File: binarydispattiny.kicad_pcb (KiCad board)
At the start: 2 copper layers, 61.8 x 40.5 mm, 32 parts, among them J1 Conn_01x02_Male, J2 Conn_01x08, J3 AVR-TPI-6, Q1 DMMT5401, U1 4021, U2 ATtiny102-SS, U3 19x12mm 7segment, U4 MAX7219, U5 19x12mm 7segment

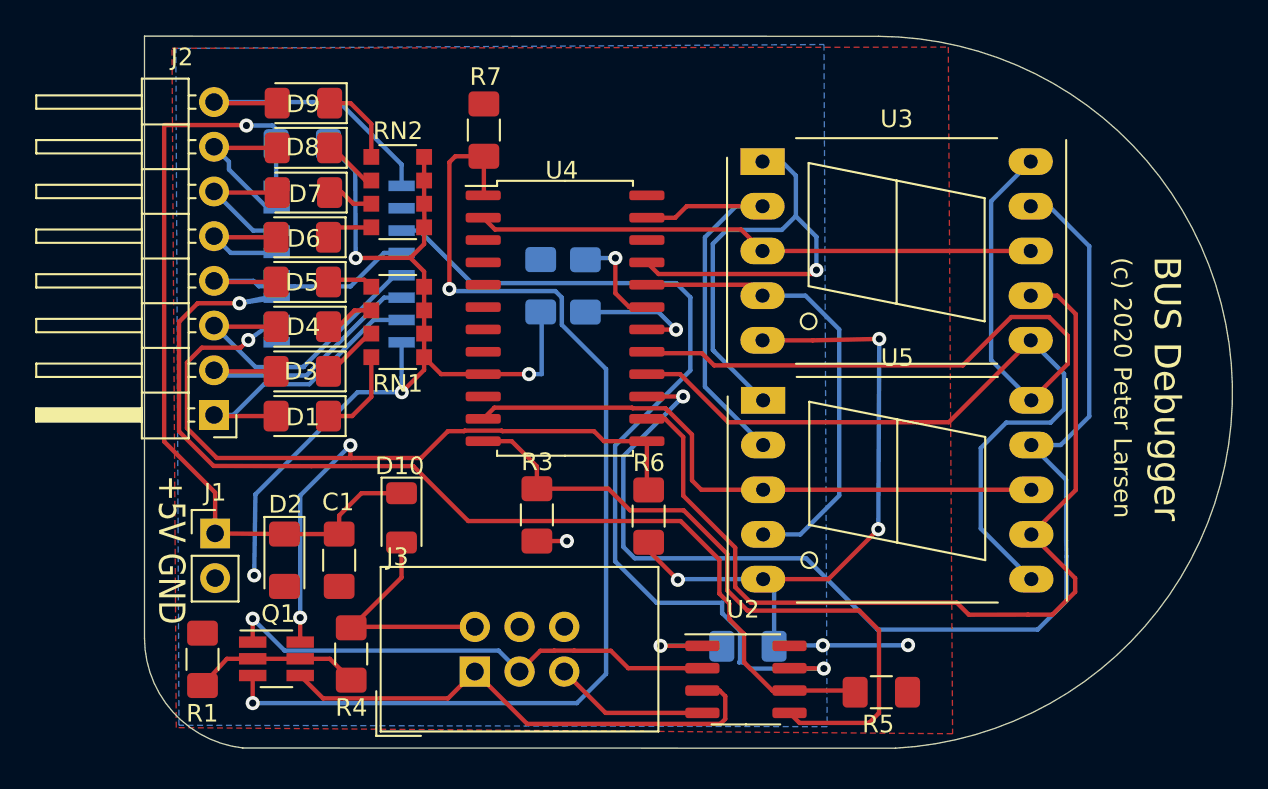
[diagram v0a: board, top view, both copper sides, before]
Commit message: Fixed MAX7912 sizing
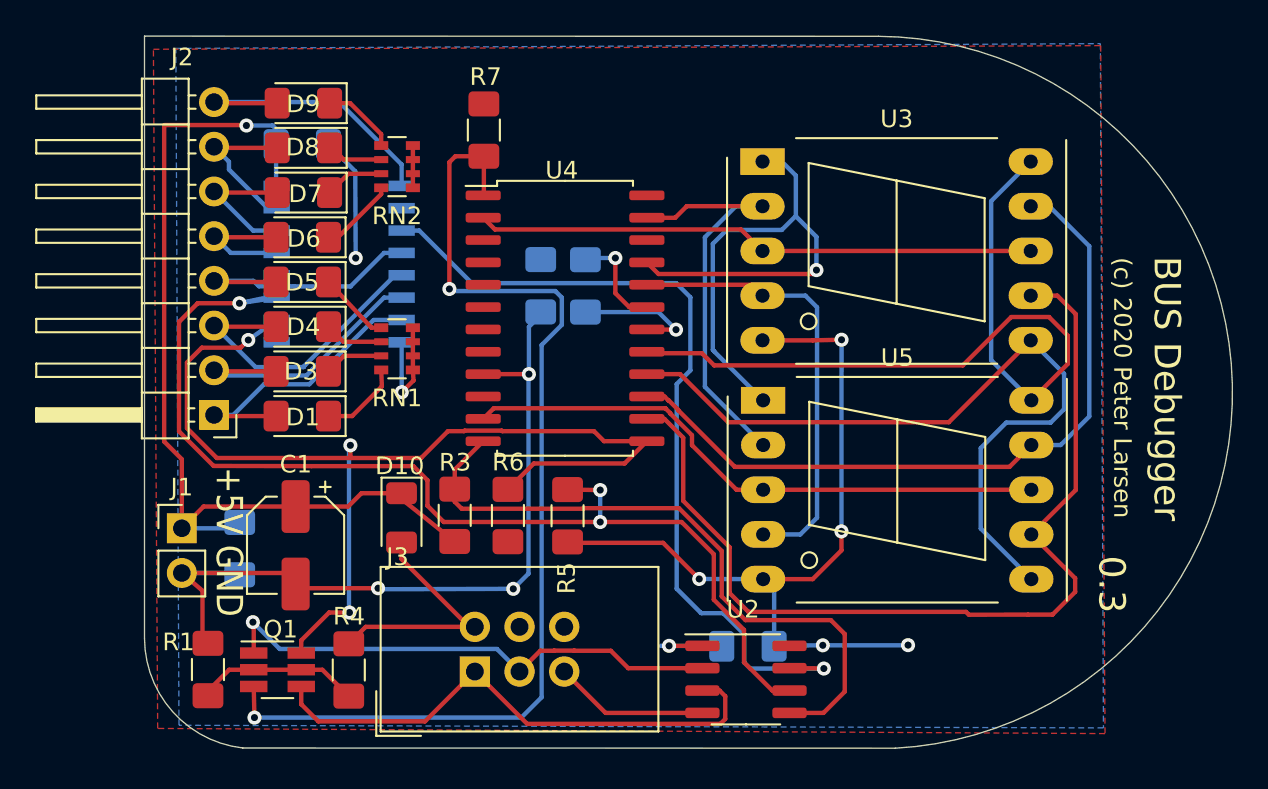
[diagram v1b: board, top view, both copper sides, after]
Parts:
- C1: footprint Capacitor_SMD:C_1206_3216Metric_Pad1.42x1.75mm_HandSolder -> Capacitor_SMD:CP_Elec_5x5.4
- D2: moved to B.Cu
- RN1, RN2: footprint Resistor_SMD:R_Array_Convex_4x1206 -> Resistor_SMD:R_Array_Convex_4x0603
- moved R5 20.5 mm to (134.3, 101.5), turned to 270 degrees
- moved R6 8.00 mm to (130.9, 101.5)
- moved R3 4.67 mm to (127.9, 101.5)
- moved D2 2.62 mm to (115.7, 103.4)
- moved C1 2.62 mm to (118.9, 103.2)
- moved J1 1.91 mm to (112.4, 102.3)
- moved RN1 1.52 mm to (124.6, 92.1)
- moved RN2 1.45 mm to (124.6, 81.7)
- moved R4 0.92 mm to (121.9, 110.3)
- moved R1 0.66 mm to (113.9, 110.3)
- moved Q1 0.63 mm to (117.8, 110.3)
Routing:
- net /SEG_F: track 67.4 -> 41.9 mm, vias 1 -> 0
- net GND: track 98.4 -> 107.3 mm, vias 9 -> 10
- net SHARED_CLK: track 53.5 -> 61.0 mm
- net +5V: track 59.9 -> 65.0 mm, vias 4 -> 3
- net INDATA: track 52.5 -> 48.0 mm
- net OUTDATA: track 63.7 -> 60.7 mm
- net Net-(D6-Pad1): track 3.44 -> 5.15 mm
- net Net-(D5-Pad1): track 2.65 -> 4.12 mm
- net TPIDATA: track 29.4 -> 30.8 mm
- net SEL_OUT: track 39.2 -> 37.8 mm
- net /DIG_1: track 34.9 -> 33.7 mm
- net /AVR-5v: track 13.2 -> 14.4 mm
- net /SEG_C: track 26.7 -> 25.6 mm
- net SEL_IN: track 60.8 -> 61.6 mm, vias 1 -> 3
- net Net-(D7-Pad1): track 2.63 -> 3.38 mm
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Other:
- board text added: "0.3"

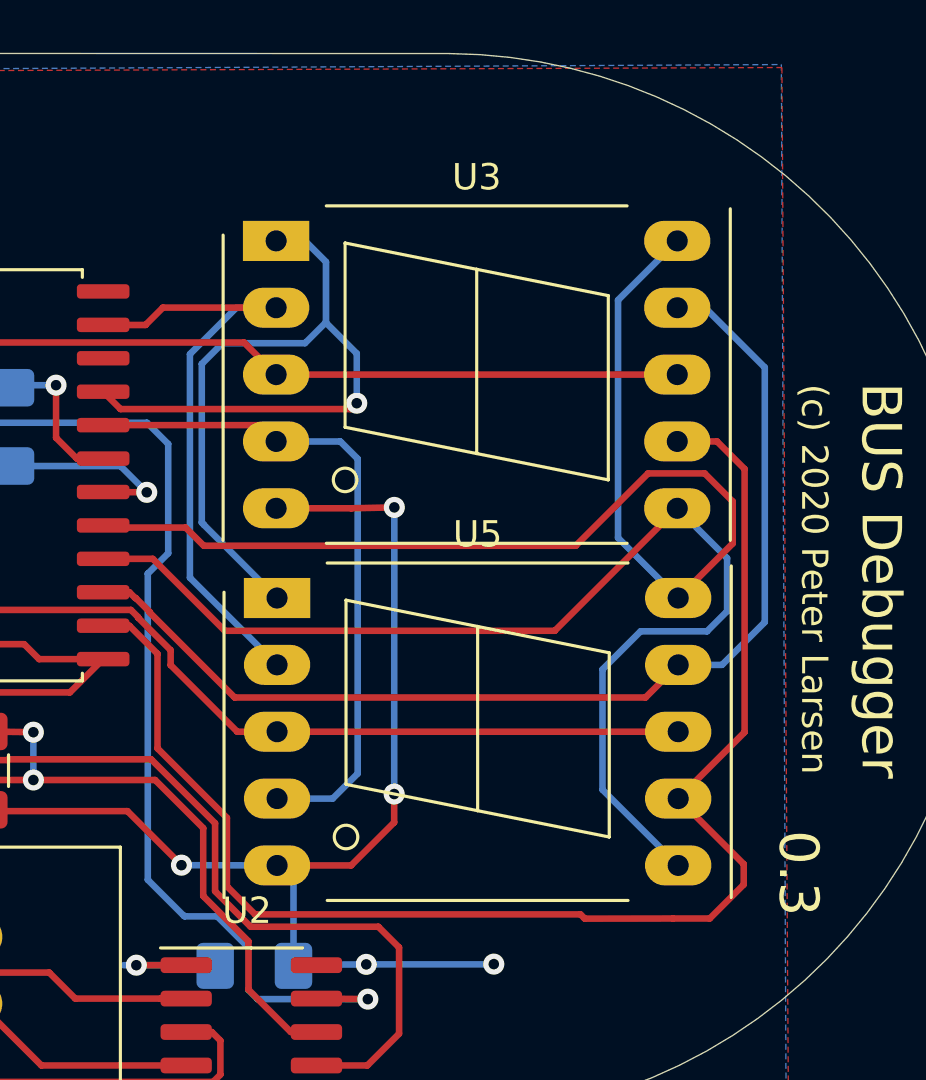
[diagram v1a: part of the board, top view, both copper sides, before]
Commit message: Fixed MAX7912 sizing #2
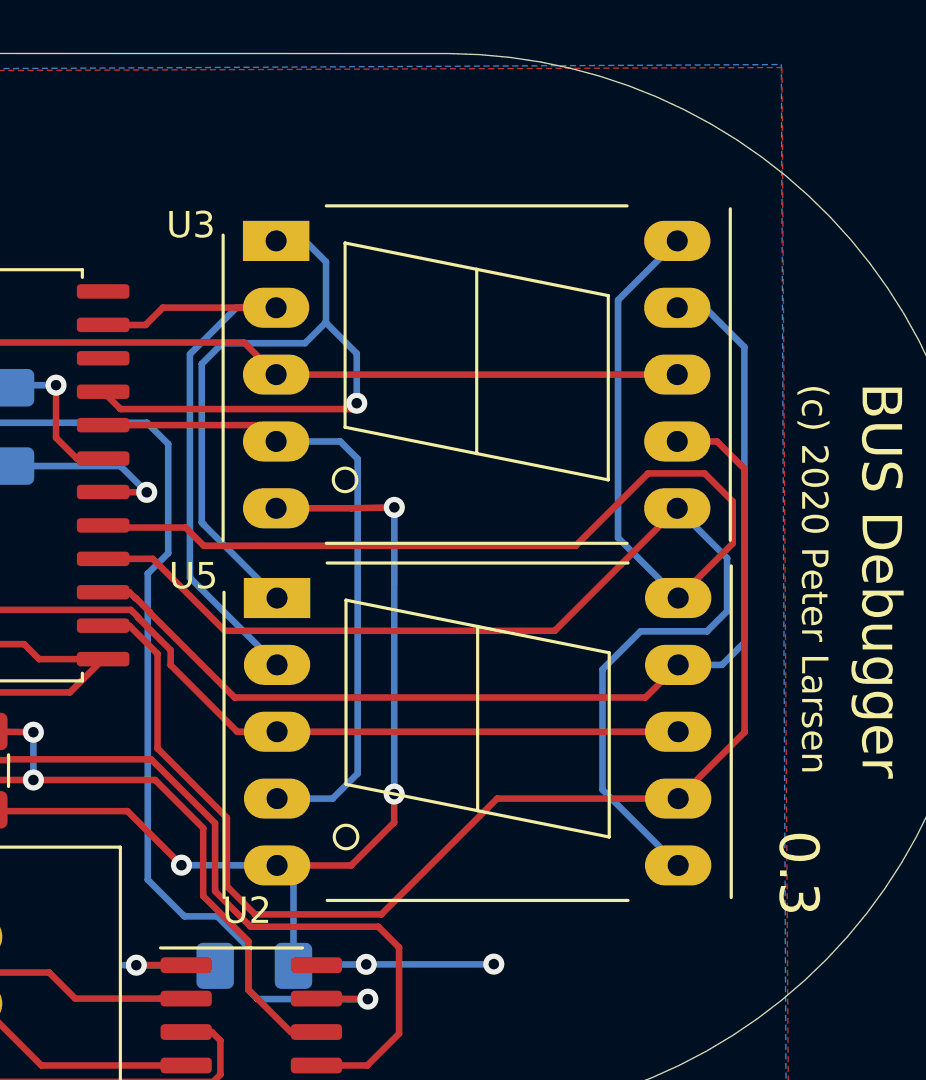
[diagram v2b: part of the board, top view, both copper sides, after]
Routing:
- net /SEG_A: track 54.0 -> 48.4 mm
- net /SEG_F: track 41.9 -> 41.3 mm
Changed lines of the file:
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@@
     (thickness 1.6)
     (drawings 10)
-    (tracks 412)
+    (tracks 408)
     (zones 0)
     (modules 32)
@@
     (descr "7-Segment Display, LTS67x0, http://optoelectronics.liteon.com/upload/download/DS30-2001-355/S6760jd.pdf")
     (tags "7Segment LED LTS6760 LTS6780")
-    (fp_text reference U5 (at 7.62 -2.42) (layer F.SilkS)
+    (fp_text reference U5 (at -3.175 -0.83312) (layer F.SilkS)
       (effects (font (size 1 1) (thickness 0.15)))
     )
@@
     (descr "7-Segment Display, LTS67x0, http://optoelectronics.liteon.com/upload/download/DS30-2001-355/S6760jd.pdf")
     (tags "7Segment LED LTS6760 LTS6780")
-    (fp_text reference U3 (at 7.62 -2.42) (layer F.SilkS)
+    (fp_text reference U3 (at -3.24104 -0.59944 180) (layer F.SilkS)
       (effects (font (size 1 1) (thickness 0.15)))
     )
@@
   (segment (start 163.203049 100.088271) (end 163.203049 90.088449) (width 0.25) (layer F.Cu) (net 31))
   (segment (start 160.6804 102.61092) (end 163.203049 100.088271) (width 0.25) (layer F.Cu) (net 31) (status 10))
-  (segment (start 161.87928 107.16768) (end 163.1696 105.87736) (width 0.25) (layer F.Cu) (net 31))
-  (segment (start 163.1696 105.10012) (end 160.6804 102.61092) (width 0.25) (layer F.Cu) (net 31))
-  (segment (start 157.13056 107.17276) (end 160.48736 107.16768) (width 0.25) (layer F.Cu) (net 31))
-  (segment (start 156.968 107.0102) (end 157.13056 107.17276) (width 0.25) (layer F.Cu) (net 31))
+  (segment (start 153.80208 102.61092) (end 160.6804 102.61092) (width 0.25) (layer F.Cu) (net 31))
+  (segment (start 149.4028 107.0102) (end 153.80208 102.61092) (width 0.25) (layer F.Cu) (net 31))
+  (segment (start 144.6022 107.0102) (end 149.4028 107.0102) (width 0.25) (layer F.Cu) (net 31))
+  (segment (start 143.5354 105.9434) (end 144.6022 107.0102) (width 0.25) (layer F.Cu) (net 31))
+  (segment (start 140.89888 100.70338) (end 143.5354 103.3399) (width 0.25) (layer F.Cu) (net 31))
+  (segment (start 140.89888 97.112101) (end 140.89888 100.70338) (width 0.25) (layer F.Cu) (net 31))
   (segment (start 143.5354 103.3399) (end 143.5354 105.9434) (width 0.25) (layer F.Cu) (net 31))
-  (segment (start 140.89888 100.70338) (end 143.5354 103.3399) (width 0.25) (layer F.Cu) (net 31))
-  (segment (start 144.6022 107.0102) (end 156.968 107.0102) (width 0.25) (layer F.Cu) (net 31))
-  (segment (start 140.89888 97.112101) (end 140.89888 100.70338) (width 0.25) (layer F.Cu) (net 31))
-  (segment (start 163.1696 105.87736) (end 163.1696 105.10012) (width 0.25) (layer F.Cu) (net 31))
   (segment (start 139.829259 96.04248) (end 140.89888 97.112101) (width 0.25) (layer F.Cu) (net 31))
-  (segment (start 160.48736 107.16768) (end 161.87928 107.16768) (width 0.25) (layer F.Cu) (net 31))
-  (segment (start 143.5354 105.9434) (end 144.6022 107.0102) (width 0.25) (layer F.Cu) (net 31))
   (segment (start 138.83312 96.04248) (end 139.829259 96.04248) (width 0.25) (layer F.Cu) (net 31))
-  (segment (start 162.34664 97.53092) (end 160.6804 97.53092) (width 0.25) (layer B.Cu) (net 32) (status 20))
-  (segment (start 163.97224 95.90532) (end 162.34664 97.53092) (width 0.25) (layer B.Cu) (net 32))
-  (segment (start 163.97224 86.233) (end 163.97224 95.90532) (width 0.25) (layer B.Cu) (net 32))
-  (segment (start 161.70148 83.96224) (end 163.97224 86.233) (width 0.25) (layer B.Cu) (net 32) (status 10))
-  (segment (start 160.64484 83.96224) (end 161.70148 83.96224) (width 0.25) (layer B.Cu) (net 32) (status 30))
   (segment (start 143.83004 98.77044) (end 159.44088 98.77044) (width 0.25) (layer F.Cu) (net 32))
   (segment (start 140.608141 95.548541) (end 143.83004 98.77044) (width 0.25) (layer F.Cu) (net 32))
@@
   (segment (start 139.83208 94.77248) (end 140.052059 94.992459) (width 0.25) (layer F.Cu) (net 32))
   (segment (start 140.608141 95.527002) (end 140.608141 95.548541) (width 0.25) (layer F.Cu) (net 32))
+  (segment (start 162.34664 97.53092) (end 160.6804 97.53092) (width 0.25) (layer B.Cu) (net 32))
+  (segment (start 163.195 96.68256) (end 162.34664 97.53092) (width 0.25) (layer B.Cu) (net 32))
+  (segment (start 163.195 85.45576) (end 163.195 96.68256) (width 0.25) (layer B.Cu) (net 32))
+  (segment (start 161.70148 83.96224) (end 163.195 85.45576) (width 0.25) (layer B.Cu) (net 32))
+  (segment (start 160.64484 83.96224) (end 161.70148 83.96224) (width 0.25) (layer B.Cu) (net 32))
   (segment (start 155.99156 96.23552) (end 160.64484 91.58224) (width 0.25) (layer F.Cu) (net 33) (status 20))
   (segment (start 143.45412 96.23552) (end 155.99156 96.23552) (width 0.25) (layer F.Cu) (net 33))

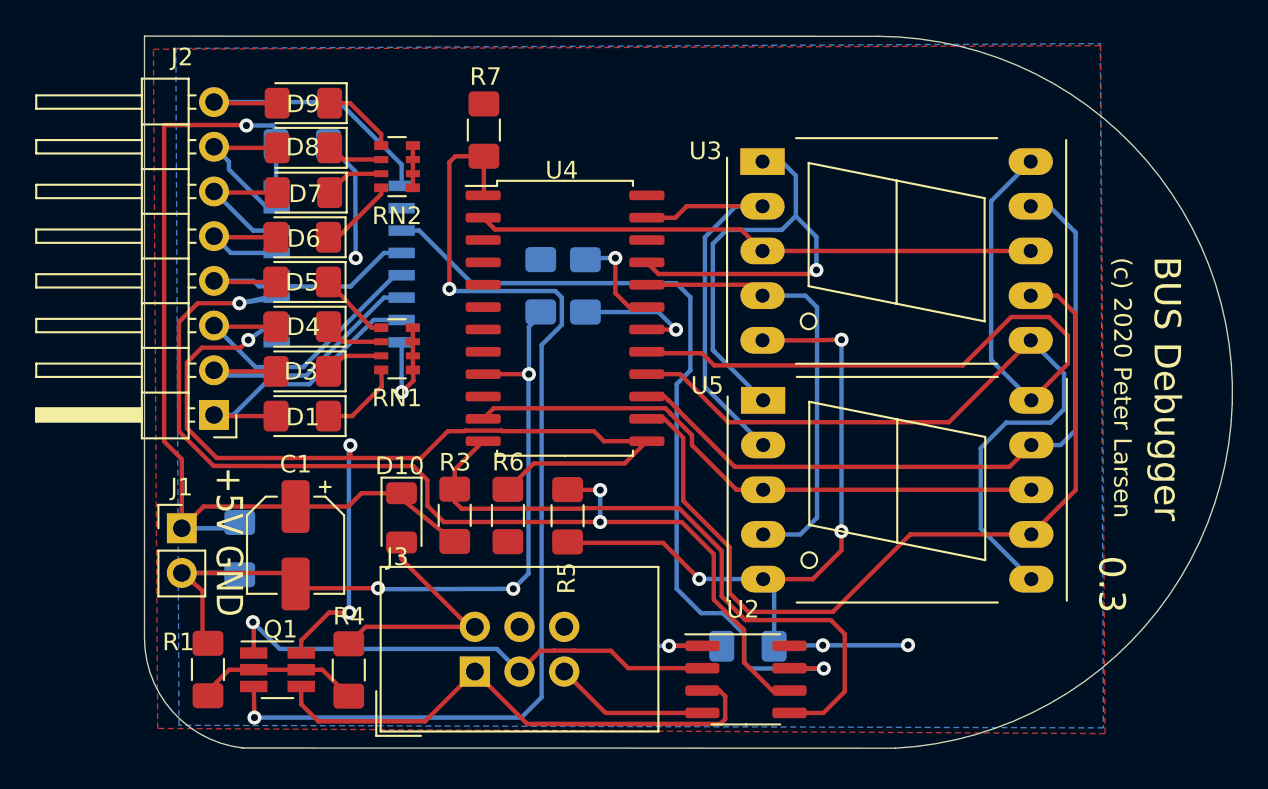
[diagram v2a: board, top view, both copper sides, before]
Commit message: Added test points
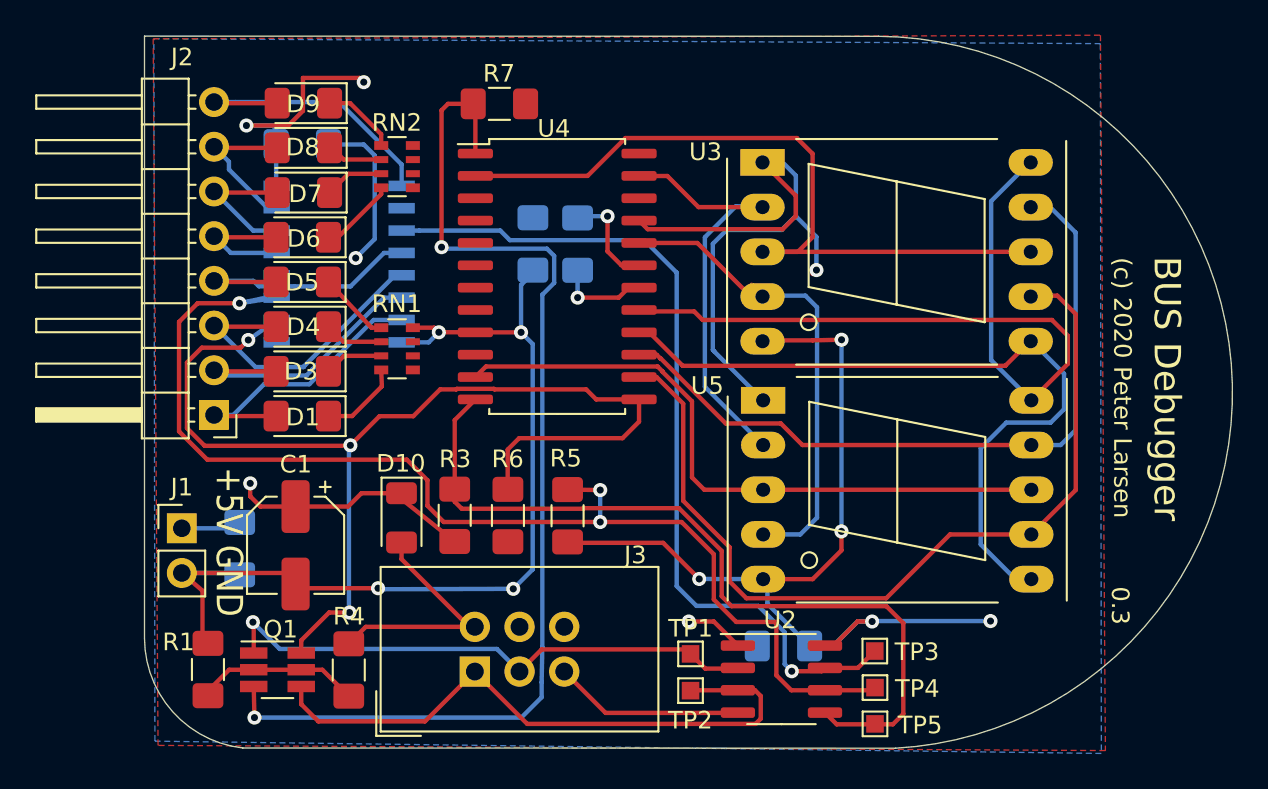
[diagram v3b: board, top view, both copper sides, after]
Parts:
- added TP1: TestPoint, TestPoint:TestPoint_Pad_1.0x1.0mm, F.Cu at (141.3, 109.4)
- added TP2: TestPoint, TestPoint:TestPoint_Pad_1.0x1.0mm, F.Cu at (141.3, 111.5)
- added TP3: TestPoint, TestPoint:TestPoint_Pad_1.0x1.0mm, F.Cu at (151.8, 109.2)
- added TP4: TestPoint, TestPoint:TestPoint_Pad_1.0x1.0mm, F.Cu at (151.8, 111.3)
- added TP5: TestPoint, TestPoint:TestPoint_Pad_1.0x1.0mm, F.Cu at (151.8, 113.4)
- moved R2 2.42 mm to (134.9, 86.1)
- moved U4 2.42 mm to (133.7, 88.0)
- moved C4 2.42 mm to (132.4, 86.1)
- moved C3 2.02 mm to (146.6, 109.0)
- moved U2 2.02 mm to (146.5, 110.8)
- moved R7 1.73 mm to (130.5, 78.1), turned to 0 degrees
- moved U3 0.05 mm to (145.4, 81.5)
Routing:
- net +5V: track 65.0 -> 40.8 mm, vias 3 -> 5
- net /DIG_0: track 31.9 -> 43.6 mm
- net GND: track 107.3 -> 116.3 mm
- net SEL_OUT: track 37.8 -> 46.3 mm
- net SEL_IN: track 61.6 -> 67.2 mm
- net TPIDATA: track 30.8 -> 35.5 mm
- net /DIG_1: track 33.7 -> 37.3 mm
- net /SEG_E: track 33.5 -> 37.1 mm
- net OUTDATA: track 60.7 -> 63.1 mm
- net /SEG_C: track 25.6 -> 27.9 mm
- net TPICLK: track 29.4 -> 31.5 mm
- net /~RST: track 8.82 -> 10.8 mm
- net Net-(R2-Pad2): track 7.22 -> 5.28 mm
- net SHARED_CLK: track 61.0 -> 62.9 mm
- net /SEG_A: track 48.4 -> 49.9 mm
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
